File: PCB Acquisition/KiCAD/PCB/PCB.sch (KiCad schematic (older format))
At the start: 5 parts

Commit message: Début du PCB avec les fichiers téléchargés d'internet
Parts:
- removed C1: 0,1 uF, symbol Device:C
- removed R1: 1k, symbol Device:R
- removed U?: Pickit_3, symbol pic:Pickit_3
- removed U?: PIC24F32KA302, symbol pic:PIC24F32KA302
- removed U?: PIC32F32KA302_carré, symbol PIC:PIC32F32KA302_carré
- added U1: PIC24F32KA302-I_SS, 24FV32KA302A:PIC24F32KA302-I&slash_SS, symbol 2020-04-10_20-01-39:PIC24F32KA302-I_SS
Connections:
- net labels removed: GND, VDD
- wire segments 24 -> 0
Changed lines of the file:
@@
 $EndDescr
 $Comp
-L pic:Pickit_3 U?
-U 1 1 5E679DE2
-P 1650 1750
-F 0 "U?" H 1687 2265 50  0000 C CNN
-F 1 "Pickit_3" H 1687 2174 50  0000 C CNN
-F 2 "" H 1650 1750 50  0001 C CNN
-F 3 "" H 1650 1750 50  0001 C CNN
-	1    1650 1750
+L 2020-04-10_20-01-39:PIC24F32KA302-I_SS U1
+U 1 1 5E90D797
+P 550 2850
+F 0 "U1" H 5850 3237 60  0000 C CNN
+F 1 "PIC24F32KA302-I_SS" H 5850 3131 60  0000 C CNN
+F 2 "24FV32KA302A:PIC24F32KA302-I&slash_SS" H 5850 3090 60  0001 C CNN
+F 3 "" H 550 2850 60  0000 C CNN
+	1    550  2850
 	1    0    0    -1
 $EndComp
-$Comp
-L pic:PIC24F32KA302 U?
-U 1 1 5E67ABEA
-P 6500 2350
-F 0 "U?" H 6525 3515 50  0000 C CNN
-F 1 "PIC24F32KA302" H 6525 3424 50  0000 C CNN
-F 2 "" H 6200 1400 50  0001 C CNN
-F 3 "" H 6200 1400 50  0001 C CNN
-	1    6500 2350
-	1    0    0    -1
-$EndComp
-$Comp
-L Device:R R1
-U 1 1 5E67C59F
-P 3250 1100
-F 0 "R1" H 3300 1150 50  0000 L CNN
-F 1 "1k" H 3300 1050 50  0000 L CNN
-F 2 "" V 3180 1100 50  0001 C CNN
-F 3 "~" H 3250 1100 50  0001 C CNN
-	1    3250 1100
-	1    0    0    -1
-$EndComp
-Wire Wire Line
-	2000 1800 2950 1800
-Wire Wire Line
-	2950 1800 2950 1900
-Wire Wire Line
-	2950 1900 3850 1900
-Wire Wire Line
-	2000 1900 2850 1900
-Wire Wire Line
-	2850 1900 2850 2050
-Wire Wire Line
-	2850 2050 3850 2050
-Wire Wire Line
-	2000 1700 2300 1700
-Wire Wire Line
-	2300 1700 2300 2500
-Wire Wire Line
-	3850 2500 2300 2500
-Connection ~ 2300 2500
-Wire Wire Line
-	2300 2500 2300 2850
-$Comp
-L power:GND #PWR?
-U 1 1 5E67D797
-P 2300 2850
-F 0 "#PWR?" H 2300 2600 50  0001 C CNN
-F 1 "GND" H 2305 2677 50  0000 C CNN
-F 2 "" H 2300 2850 50  0001 C CNN
-F 3 "" H 2300 2850 50  0001 C CNN
-	1    2300 2850
-	1    0    0    -1
-$EndComp
-Wire Wire Line
-	2000 1600 2750 1600
-Wire Wire Line
-	2750 1600 2750 3250
-Wire Wire Line
-	2750 3250 3850 3250
-$Comp
-L power:VDD #PWR?
-U 1 1 5E67E00B
-P 3250 800
-F 0 "#PWR?" H 3250 650 50  0001 C CNN
-F 1 "VDD" H 3267 973 50  0000 C CNN
-F 2 "" H 3250 800 50  0001 C CNN
-F 3 "" H 3250 800 50  0001 C CNN
-	1    3250 800
-	1    0    0    -1
-$EndComp
-Wire Wire Line
-	2000 1500 2000 1450
-Wire Wire Line
-	2000 1450 3250 1450
-Wire Wire Line
-	3250 1250 3250 1450
-Connection ~ 3250 1450
-Wire Wire Line
-	3250 1450 3850 1450
-Wire Wire Line
-	3250 800  3250 950
-$Comp
-L Device:C C1
-U 1 1 5E6AB898
-P 9550 1500
-F 0 "C1" H 9665 1546 50  0000 L CNN
-F 1 "0,1 uF" H 9665 1455 50  0000 L CNN
-F 2 "" H 9588 1350 50  0001 C CNN
-F 3 "~" H 9550 1500 50  0001 C CNN
-	1    9550 1500
-	1    0    0    -1
-$EndComp
-Wire Wire Line
-	9200 1450 9350 1450
-Wire Wire Line
-	9350 1450 9350 1350
-Wire Wire Line
-	9350 1350 9550 1350
-Wire Wire Line
-	9200 1600 9400 1600
-Wire Wire Line
-	9400 1600 9400 1650
-Wire Wire Line
-	9400 1650 9550 1650
-$Comp
-L PIC:PIC32F32KA302_carré U?
-U 1 1 5E91735C
-P 4250 5750
-F 0 "U?" H 7044 5696 50  0000 L CNN
-F 1 "PIC32F32KA302_carré" H 7044 5605 50  0000 L CNN
-F 2 "" H 4800 5650 50  0001 C CNN
-F 3 "" H 4800 5650 50  0001 C CNN
-	1    4250 5750
-	1    0    0    -1
-$EndComp

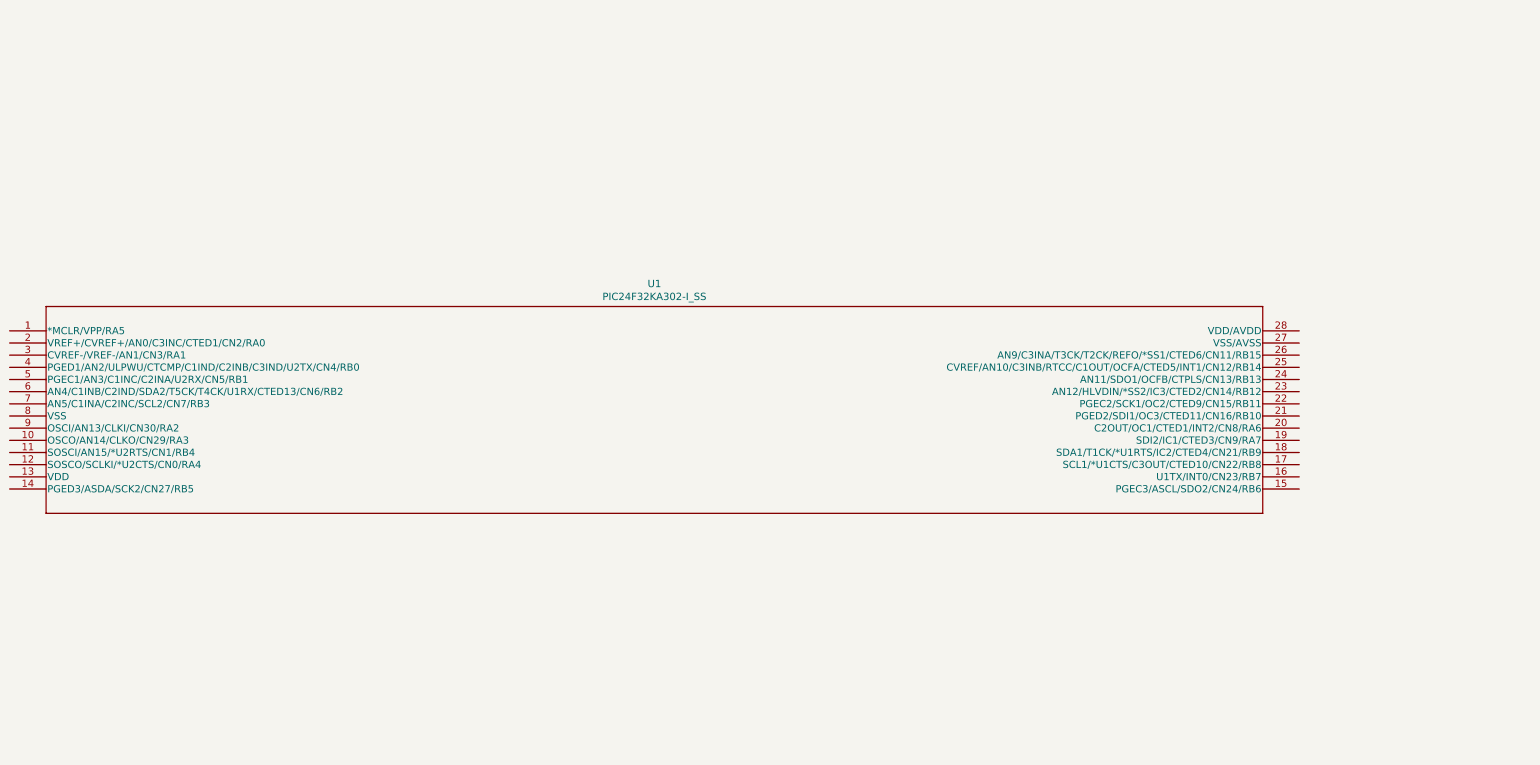
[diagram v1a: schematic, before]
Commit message: Développement du PCB
Ajout du pickit au schéma et début du circuit
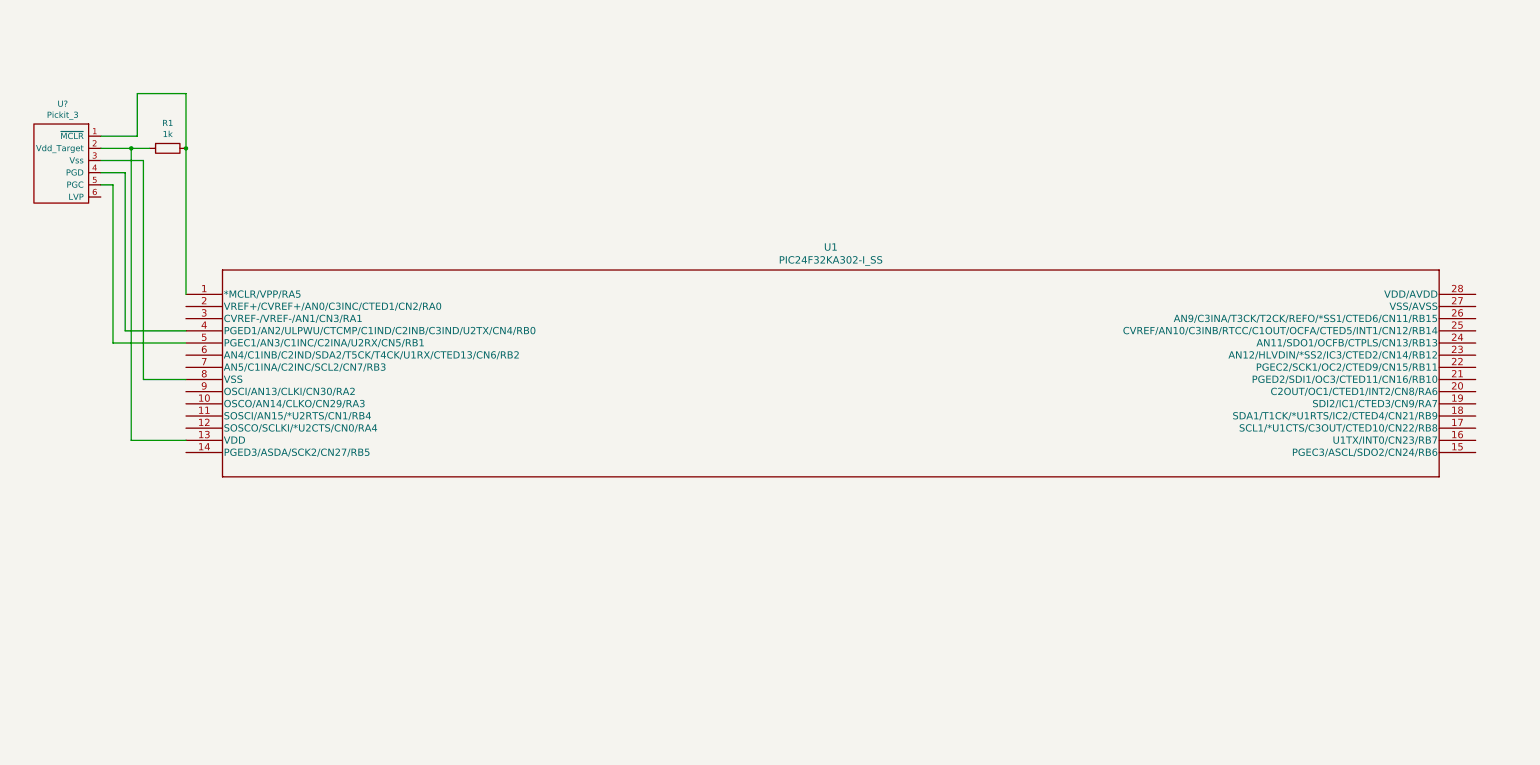
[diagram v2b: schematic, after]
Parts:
- added R1: 1k, symbol Device:R
- added U?: Pickit_3, symbol PIC:Pickit_3
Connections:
- net at U1.1 (*MCLR/VPP/RA5): now also R1.1, U?.1 (~MCLR)
- net at U1.13 (VDD): now also R1.2, U?.2 (Vdd_Target)
- net at U1.4 (PGED1/AN2/ULPWU/CTCMP/C1IND/C2INB/C3IND/U2TX/CN4/RB0): now also U?.4 (PGD)
- net at U1.5 (PGEC1/AN3/C1INC/C2INA/U2RX/CN5/RB1): now also U?.5 (PGC)
- net at U1.8 (VSS): now also U?.3 (Vss)
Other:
- moved on the sheet: U1
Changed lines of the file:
@@
 L 2020-04-10_20-01-39:PIC24F32KA302-I_SS U1
 U 1 1 5E90D797
-P 550 2850
-F 0 "U1" H 5850 3237 60  0000 C CNN
-F 1 "PIC24F32KA302-I_SS" H 5850 3131 60  0000 C CNN
-F 2 "24FV32KA302A:PIC24F32KA302-I&slash_SS" H 5850 3090 60  0001 C CNN
-F 3 "" H 550 2850 60  0000 C CNN
-	1    550  2850
+P 2000 2550
+F 0 "U1" H 7300 2937 60  0000 C CNN
+F 1 "PIC24F32KA302-I_SS" H 7300 2831 60  0000 C CNN
+F 2 "24FV32KA302A:PIC24F32KA302-I&slash_SS" H 7300 2790 60  0001 C CNN
+F 3 "" H 2000 2550 60  0000 C CNN
+	1    2000 2550
 	1    0    0    -1
 $EndComp
+$Comp
+L PIC:Pickit_3 U?
+U 1 1 5F6DC992
+P 950 1500
+F 0 "U?" H 987 2015 50  0000 C CNN
+F 1 "Pickit_3" H 987 1924 50  0000 C CNN
+F 2 "" H 950 1500 50  0001 C CNN
+F 3 "" H 950 1500 50  0001 C CNN
+	1    950  1500
+	1    0    0    -1
+$EndComp
+Wire Wire Line
+	1300 1550 1500 1550
+Wire Wire Line
+	1500 1550 1500 2850
+Wire Wire Line
+	1500 2850 2000 2850
+Wire Wire Line
+	1300 1650 1400 1650
+Wire Wire Line
+	1400 1650 1400 2950
+Wire Wire Line
+	1400 2950 2000 2950
+Wire Wire Line
+	1300 1450 1650 1450
+Wire Wire Line
+	1650 1450 1650 3250
+Wire Wire Line
+	1650 3250 2000 3250
+Wire Wire Line
+	1300 1350 1550 1350
+Wire Wire Line
+	1550 1350 1550 3750
+Wire Wire Line
+	1550 3750 2000 3750
+$Comp
+L Device:R R1
+U 1 1 5F6DF8B5
+P 1850 1350
+F 0 "R1" V 1643 1350 50  0000 C CNN
+F 1 "1k" V 1734 1350 50  0000 C CNN
+F 2 "" V 1780 1350 50  0001 C CNN
+F 3 "~" H 1850 1350 50  0001 C CNN
+	1    1850 1350
+	0    1    1    0
+$EndComp
+Wire Wire Line
+	1550 1350 1700 1350
+Connection ~ 1550 1350
+Wire Wire Line
+	1300 1250 1600 1250
+Wire Wire Line
+	1600 1250 1600 900
+Wire Wire Line
+	1600 900  2000 900
+Wire Wire Line
+	2000 900  2000 1350
+Wire Wire Line
+	2000 2550 2000 1350
+Connection ~ 2000 1350
 $EndSCHEMATC

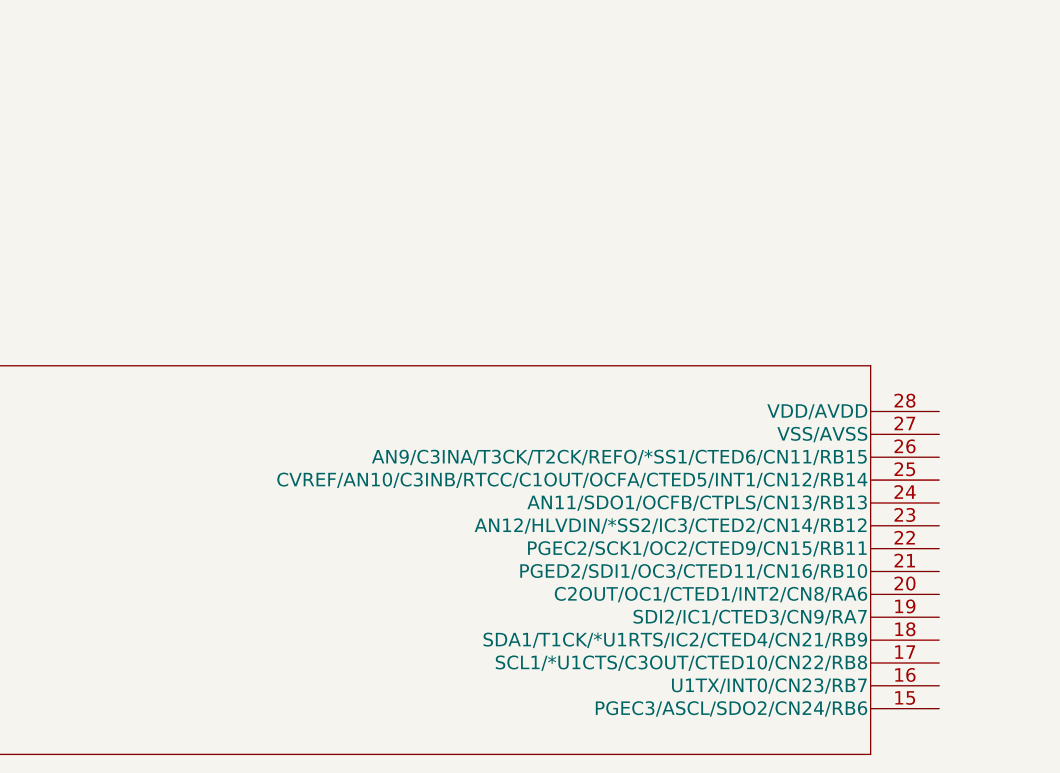
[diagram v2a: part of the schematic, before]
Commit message: Ajout des connections pour I2C sur le schéma
Ajout des connections pour I2C SCL et SDA sur le schéma
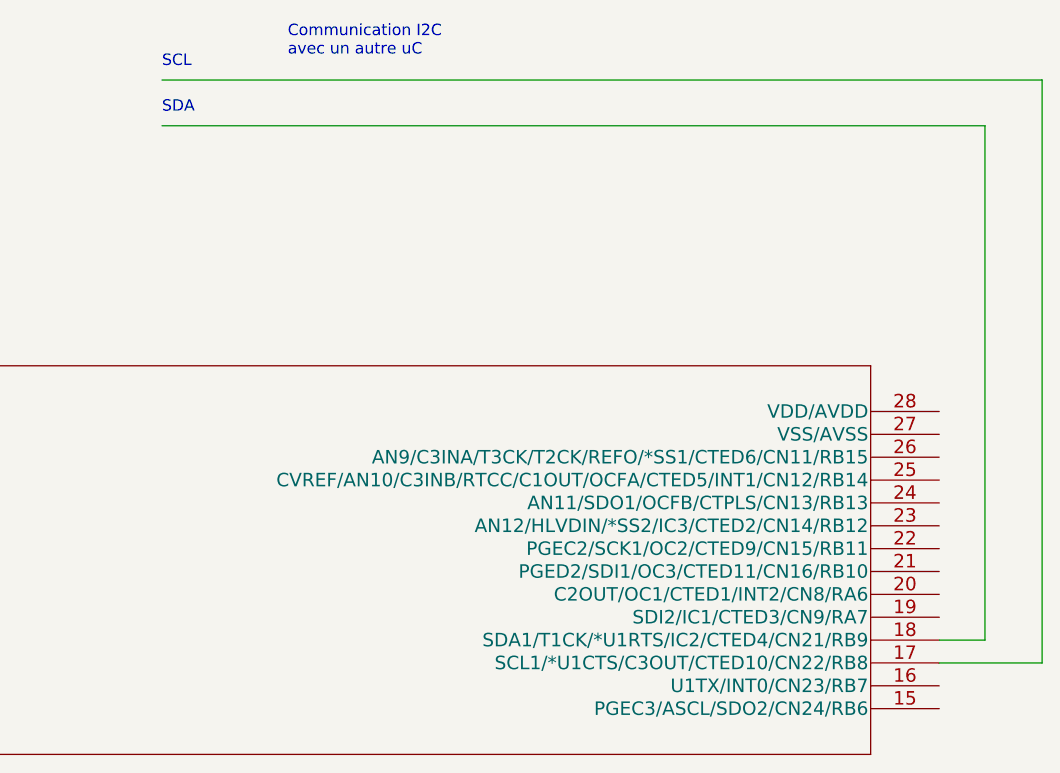
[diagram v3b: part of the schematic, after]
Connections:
- wire segments 18 -> 24
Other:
- note added: "Communication I2C\navec un autre uC"
- note added: "SCL\n"
- note added: "SDA"
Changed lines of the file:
@@
 	2000 2550 2000 1350
 Connection ~ 2000 1350
+Wire Wire Line
+	12800 1300 12800 3550
+Wire Wire Line
+	12800 3550 12600 3550
+Wire Wire Line
+	9200 1300 12800 1300
+Wire Wire Line
+	12600 3650 13050 3650
+Wire Wire Line
+	13050 3650 13050 1100
+Wire Wire Line
+	13050 1100 9200 1100
+Text Notes 9750 1000 0    50   ~ 0
+Communication I2C\navec un autre uC
+Text Notes 9200 1050 0    50   ~ 0
+SCL\n
+Text Notes 9200 1250 0    50   ~ 0
+SDA
 $EndSCHEMATC

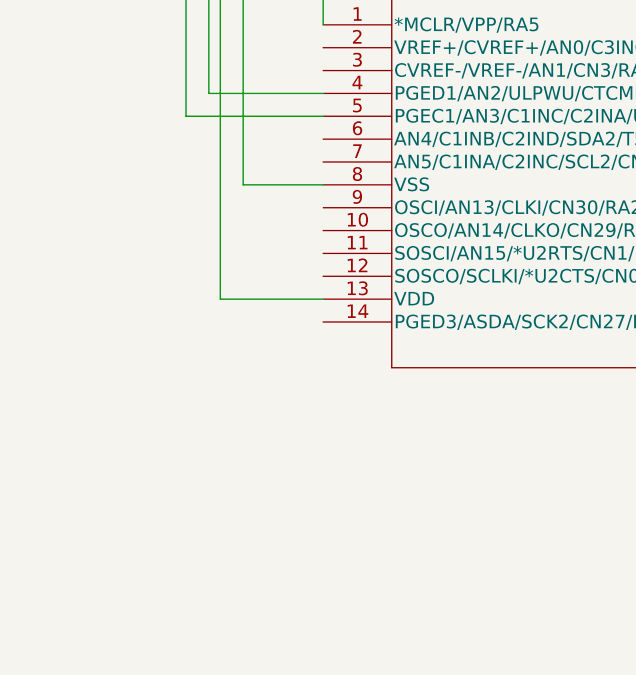
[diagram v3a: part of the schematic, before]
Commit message: Ajout de l'électrode au schéma
Les connexions nécessaires pour lier le PIC et l'électrode ont été ajoutées au schéma
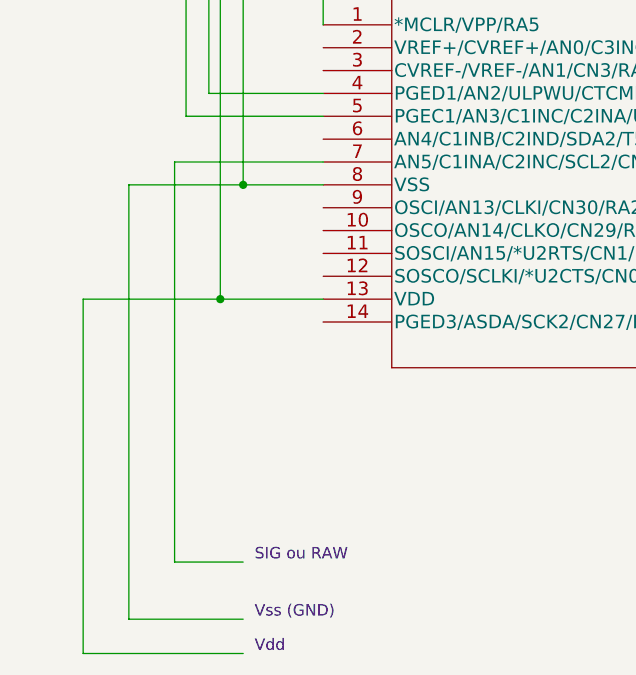
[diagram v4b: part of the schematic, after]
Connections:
- wire segments 24 -> 33
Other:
- note added: "SIG ou RAW"
- note added: "Vdd"
- note added: "Vss (GND)\n"
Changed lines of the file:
@@
 Text Notes 9200 1250 0    50   ~ 0
 SDA
+Wire Wire Line
+	2000 3150 1350 3150
+Wire Wire Line
+	1350 3150 1350 4900
+Wire Wire Line
+	1350 4900 1650 4900
+Text Notes 1700 4900 0    50   ~ 0
+SIG ou RAW
+Wire Wire Line
+	1650 3250 1150 3250
+Wire Wire Line
+	1150 3250 1150 5150
+Wire Wire Line
+	1150 5150 1650 5150
+Connection ~ 1650 3250
+Wire Wire Line
+	1550 3750 950  3750
+Wire Wire Line
+	950  3750 950  5300
+Wire Wire Line
+	950  5300 1650 5300
+Connection ~ 1550 3750
+Text Notes 1700 5150 0    50   ~ 0
+Vss (GND)\n
+Text Notes 1700 5300 0    50   ~ 0
+Vdd
 $EndSCHEMATC
